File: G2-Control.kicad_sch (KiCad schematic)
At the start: 96 parts, among them J1 Conn_01x06_Pin, J102 Conn_01x06_Pin, J103 Conn_01x06_Pin, J104 Board Interconnect, J2 Q2_link, J3 Conn_01x07_Pin, J4 Conn_01x05_Pin, K1 AZ822-2C-24DSE, K2 AZ822-2C-24DSE, K3 AZ822-2C-24DSE, Q1 TIP122, Q2 IRF840BPF, Q3 2N5061, Q4 2N4403, Q5 BC847, Q6 IRF9530N, U1 LM317L_SOT89, U2 uA748, U3 4N36, U4 78L05, U5 LMC555CMX

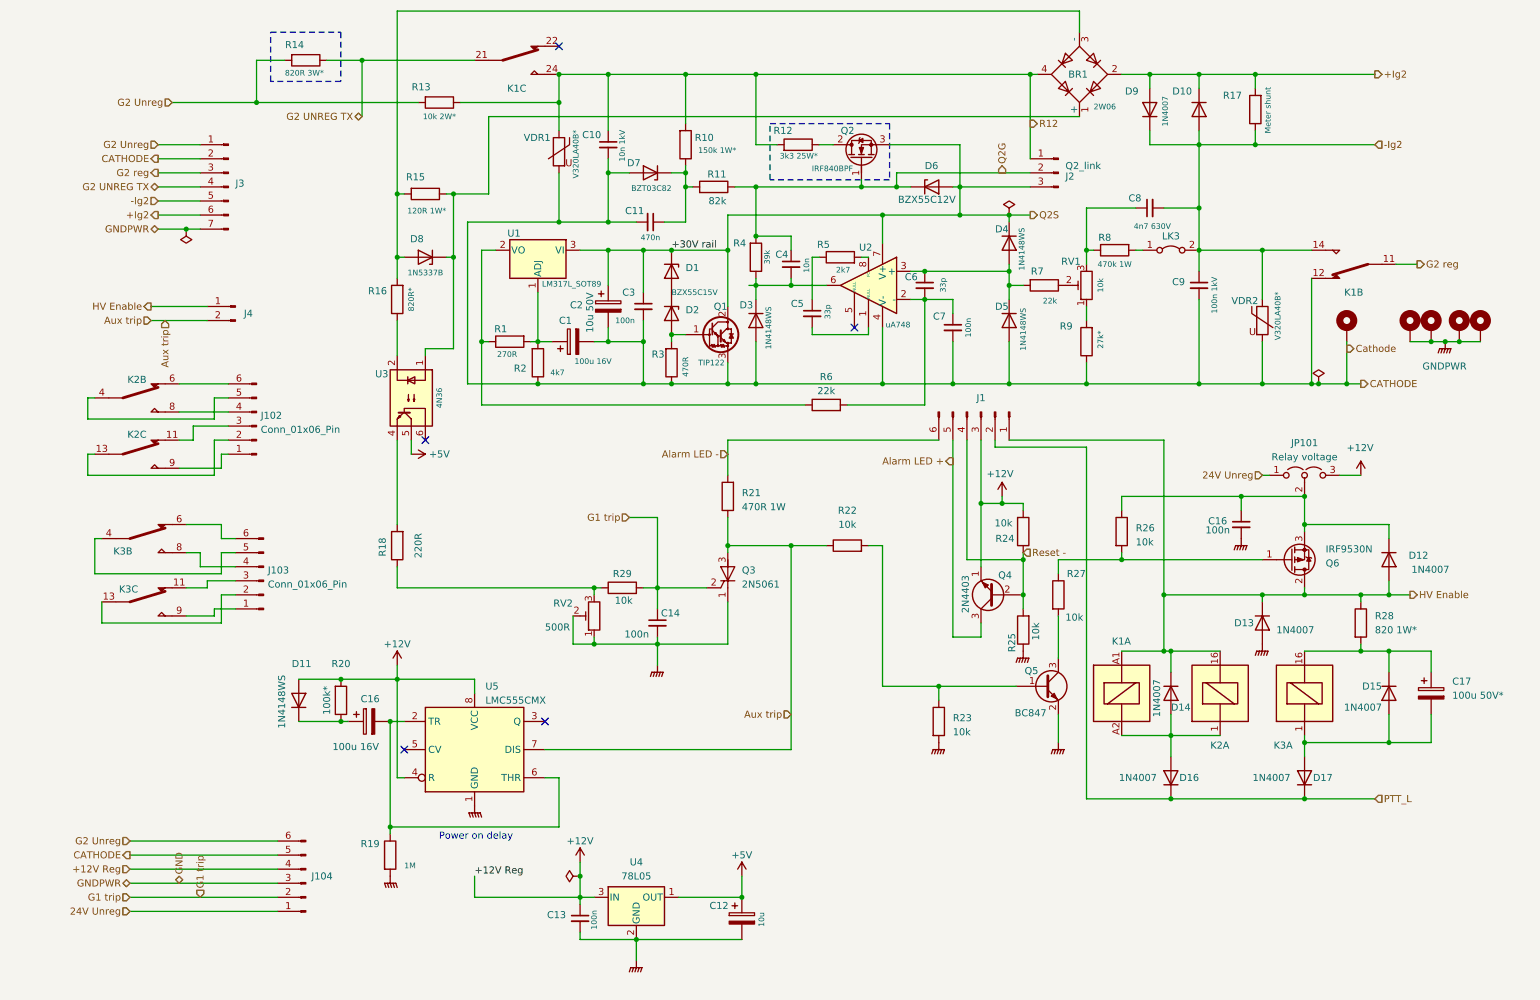
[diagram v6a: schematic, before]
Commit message: Updated format to KiCad 9. Included footprints etc.
Standardized PCB layers, updated property formatting, and adjusted net assignments. Added some DigiKey, Electrokit, and Mouser component part numbers.
Reduced font sizes for better readability and incorporated embedded font settings.
Removed the sequencer from the schematic which wasn't really meant to be there.
Revised and excluded drc and erc warnings and exclusions.
Included footprints into the project library that formerly was defined outside of the project.
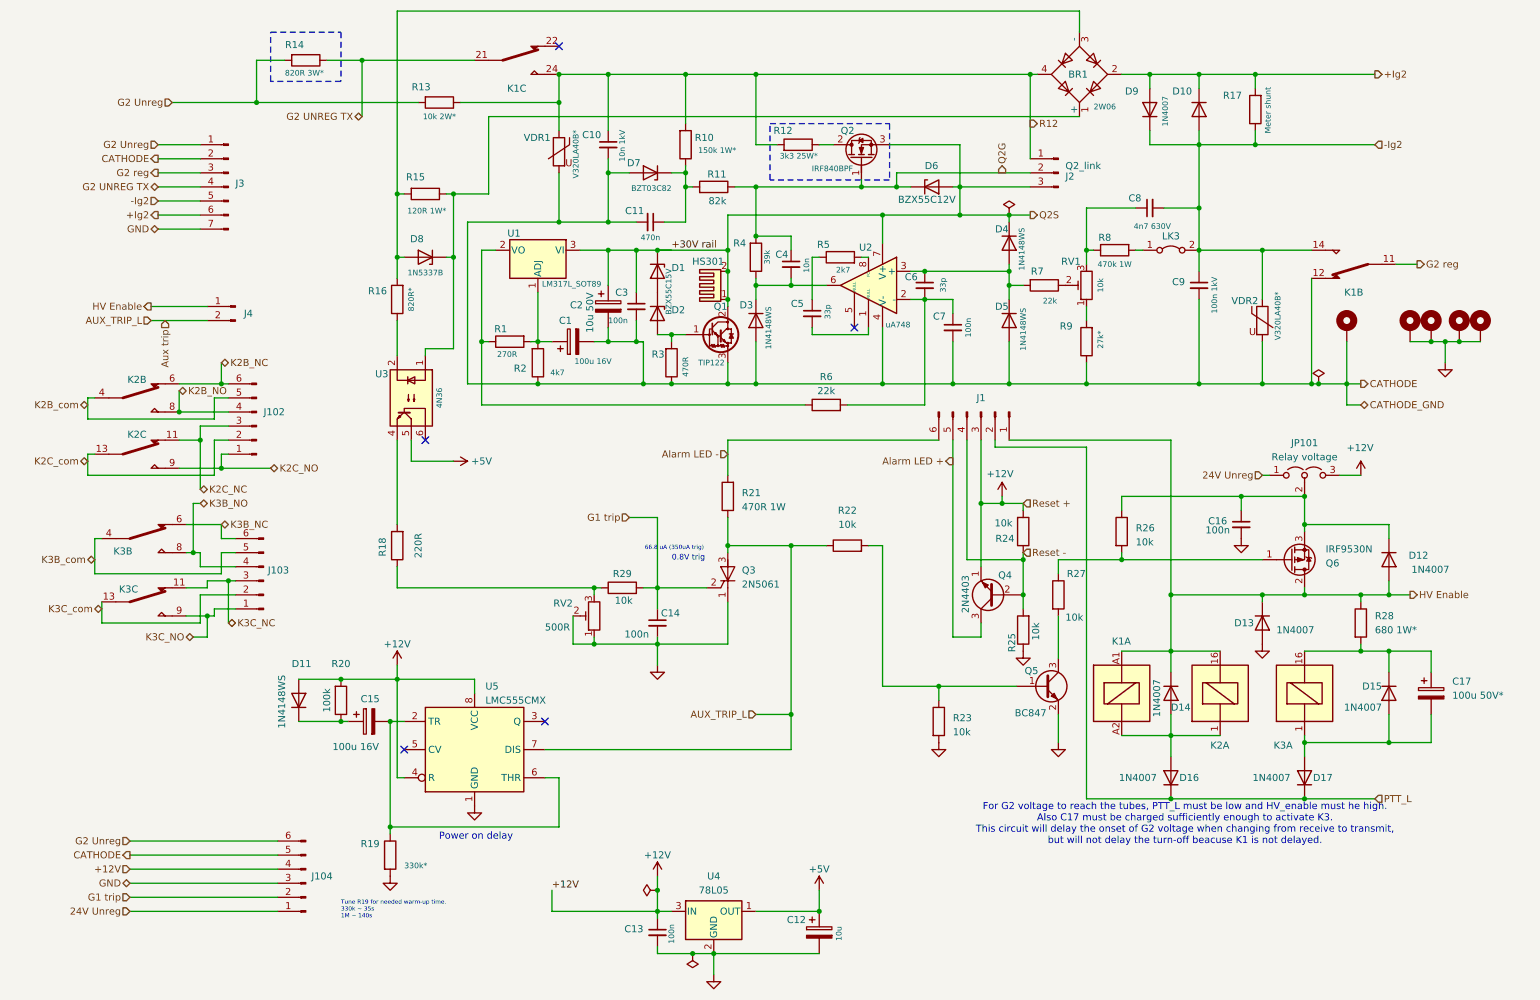
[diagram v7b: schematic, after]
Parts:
- added HS301: Heatsink_Pad_2Pin, Project_library:6025DG_Cooler, symbol Mechanical:Heatsink_Pad_2Pin
- BR1: Electrokit # (none) -> 40310051; Order # 40310051 -> (none); SMD (none) -> 0; Supplier Electrokit -> (none)
- C1: Electrokit # (none) -> 41013566; Order # 41013566 -> (none); SMD (none) -> 1; Supplier Electrokit -> (none)
- C10: Electrokit # (none) -> 41015195; Order # 41015195 -> (none); SMD (none) -> 0; Supplier Electrokit -> (none)
- C11: Electrokit # (none) -> 40502115; Mouser # (none) -> 963-HMK212C7474MGHTE; Order # 40502115 -> (none); SMD (none) -> 1; Supplier Electrokit -> (none)
- C12: Electrokit # (none) -> 40503063; Mouser # (none) -> 187-CL31A106KAHNFNE; Order # 40503063 -> (none); SMD (none) -> 1; Supplier Electrokit -> (none)
- C13, C14, C16, C3, C7: Electrokit # (none) -> 40503054; Mouser # (none) -> 80-C1206C104M5R; Order # 40503054 -> (none); SMD (none) -> 1; Supplier Electrokit -> (none)
- C15: renamed from C16; Electrokit # (none) -> 41013566; Order # 41013566 -> (none); SMD (none) -> 1; Supplier Electrokit -> (none)
- C17: SMD (none) -> 0; Supplier Electrokit* -> (none)
- C2: Electrokit # (none) -> 41015482; Order # 41015482 -> (none); SMD (none) -> 1; Supplier Electrokit -> (none)
- C4: Electrokit # (none) -> 40502095; Order # 40502095 -> (none); SMD (none) -> 1; Supplier Electrokit -> (none)
- C5, C6: Electrokit # (none) -> 40502045; Order # 40502045 -> (none); SMD (none) -> 1; Supplier Electrokit -> (none)
- C8: Electrokit # (none) -> 41016833; Order # 41016833 -> (none); SMD (none) -> 0; Supplier Electrokit -> (none)
- C9: Electrokit # (none) -> 41016939; Order # 41016939 -> (none); SMD (none) -> 0; Supplier Electrokit -> (none)
- D1, D2: Electrokit # (none) -> 40310036; Order # 40310036 -> (none); SMD (none) -> 0; Supplier Electrokit -> (none)
- D10, D12, D13, D14, D15, D16, D17, D9: Electrokit # (none) -> 40310007; Order # 40310007 -> (none); SMD (none) -> 0; Supplier Electrokit -> (none)
- D11, D3, D4, D5: Electrokit # (none) -> 41011670; Order # 41011670 -> (none); SMD (none) -> 1; Supplier Electrokit -> (none)
- D6: Electrokit # (none) -> 40310033; Order # 40310033 -> (none); SMD (none) -> 0; Supplier Electrokit -> (none)
- D7: DigiKey # (none) -> 112-BZT03C82-CT-ND; Order # 112-BZT03C82-CT-ND -> (none); SMD (none) -> 0; Supplier DigiKey -> (none)
- D8: DigiKey # (none) -> 1N5337BGOS-ND; Order # 1N5337BGOS-ND -> (none); SMD (none) -> 0; Supplier DigiKey -> (none)
- H1, H2, H3, H4, H5: Electrokit # (none) -> ----; Order # ---- -> (none); SMD (none) -> 0; Supplier Elecrow -> (none)
- J1, J102, J103: Electrokit # (none) -> 41017488; Order # 41017488 -> (none); SMD (none) -> 0; Supplier Electrokit -> (none)
- J104: value Board Interconnect -> Board Interconnect; Electrokit # (none) -> 41017488; Order # 41017488 -> (none); SMD (none) -> 0; Supplier Electrokit -> (none)
- J2: Electrokit # (none) -> 40210022; Order # 40210022 -> (none); SMD (none) -> 0; Supplier Electrokit -> (none)
- J3: DigiKey # (none) -> 277-1155-ND; Order # 277-1155-ND -> (none); SMD (none) -> 0; Supplier DigiKey -> (none)
- J4: Electrokit # (none) -> 40210021; Order # 40210021 -> (none); SMD (none) -> 0; Supplier Electrokit -> (none)
- JP101: Electrokit # (none) -> 41010445; Order # 41010445 -> (none); SMD (none) -> 0; Supplier Electrokit -> (none)
- K1: value AZ822-2C-24DSE -> Schrack RTE24024; Electrokit # (none) -> 41016807; Mouser # (none) -> 655-RTE24024; Order # 3385-AZ822-2C-24DSE-ND -> (none); SMD (none) -> 0; Supplier DigiKey -> (none)
- K2: DigiKey # (none) -> 3385-AZ822-2C-24DSE-ND; Order # 3385-AZ822-2C-24DSE-ND -> (none); SMD (none) -> 0; Supplier DigiKey -> (none)
- K3: SMD (none) -> 0
- LK3: Electrokit # (none) -> ----; Order # ---- -> (none); SMD (none) -> 0; Supplier Me (wire) -> (none)
- Q1: Electrokit # (none) -> 40320122; Order # 40320122 -> (none); SMD (none) -> 0; Supplier Electrokit -> (none)
- Q2: Electrokit # (none) -> 41011818; Order # 41011818 -> (none); SMD (none) -> 0; Supplier Electrokit -> (none)
- Q3: footprint Package_TO_SOT_THT:TO-92S_Wide -> Project_library:TO-92S_Wide; Electrokit # (none) -> 41017550; Order # 41017550 -> (none); SMD (none) -> 0; Supplier Electrokit -> (none)
- Q4: Electrokit # (none) -> 41011150; Order # 41011150 -> (none); SMD (none) -> 0; Supplier Electrokit -> (none)
- Q5: Electrokit # (none) -> 40320013; Order # 40320013 -> (none); SMD (none) -> 1; Supplier Electrokit -> (none)
- Q6: Electrokit # (none) -> 41015917; Order # 41015917 -> (none); SMD (none) -> 0; Supplier Electrokit -> (none)
- R1: Electrokit # (none) -> 40818227; Order # 40818227 -> (none); SMD (none) -> 1; Supplier Electrokit -> (none)
- R10: DigiKey # (none) -> 150KWCT-ND; Order # 150KWCT-ND -> (none); SMD (none) -> 0; Supplier DigiKey -> (none)
- R11: Electrokit # (none) -> 40818482; Mouser # (none) -> 667-ERJ-P08J823V; Order # 40818482 -> (none); SMD (none) -> 1; Supplier Electrokit -> (none)
- R12: DigiKey # (none) -> A132004-ND; Order # A132004-ND -> (none); SMD (none) -> 0; Supplier DigiKey -> (none)
- R13: DigiKey # (none) -> 10KZCT-ND; Order # 10KZCT-ND -> (none); SMD (none) -> 0; Supplier DigiKey -> (none)
- R14: DigiKey # (none) -> KAL50FB1K00-ND*; Order # KAL50FB1K00-ND* -> (none); SMD (none) -> 0; Supplier DigiKey* -> (none)
- R15: DigiKey # (none) -> PPC82W-1CT-ND* KAL50FB1K00-ND* F3039-ND LMC555CMXCT-ND 296-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; Order # PPC82W-1CT-ND* -> (none); SMD (none) -> 0; Supplier DigiKey* -> (none)
- R16: Electrokit # (none) -> 40818315; Order # 40818315 -> (none); SMD (none) -> 1; Supplier Electrokit -> (none)
- R17: SMD (none) -> 1
- R18: Electrokit # (none) -> 40818222; Order # 40818222 -> (none); SMD (none) -> 1; Supplier Electrokit -> (none)
- R19: value 1M -> 330k*; Electrokit # (none) -> 40818610; Mouser # (none) -> 279-CRGP1206F1M0; Order # 40818610 -> (none); SMD (none) -> 1; Supplier Electrokit -> (none)
- R2: Electrokit # (none) -> 40818347; Mouser # (none) -> 603-RC1206FR-074K7L; Order # 40818347 -> (none); SMD (none) -> 1; Supplier Electrokit -> (none)
- R20: value 100k* -> 100k; Electrokit # (none) -> 40818510; Order # 40818510 -> (none); SMD (none) -> 1; Supplier Electrokit -> (none)
- R21: DigiKey # (none) -> 13-FMP100JT-52-470RCT-ND; Order # 13-FMP100JT-52-470RCT-ND -> (none); SMD (none) -> 0; Supplier DigiKey -> (none)
- R22, R23, R24, R25, R26, R27, R29: Electrokit # (none) -> 40818410; Order # 40818410 -> (none); SMD (none) -> 1; Supplier Electrokit -> (none)
- R28: value 820 1W* -> 680 1W*; SMD (none) -> 0
- R3: Electrokit # (none) -> 40818247; Mouser # (none) -> 603-AF1206JR-07470RL; Order # 40818247 -> (none); SMD (none) -> 1; Supplier Electrokit -> (none)
- R4: Electrokit # (none) -> 40818439; Mouser # (none) -> 603-RC1206JR-0739KL; Order # 40818439 -> (none); SMD (none) -> 1; Supplier Electrokit -> (none)
- R5: Electrokit # (none) -> 40818327; Mouser # (none) -> 652-CR1206FX-2701ELF; Order # 40818327 -> (none); SMD (none) -> 1; Supplier Electrokit -> (none)
- R6, R7: Electrokit # (none) -> 40818422; Mouser # (none) -> 71-CRCW1206-22K-E3; Order # 40818422 -> (none); SMD (none) -> 1; Supplier Electrokit -> (none)
- R8: DigiKey # (none) -> 470KWCT-ND; Order # 470KWCT-ND -> (none); SMD (none) -> 0; Supplier DigiKey -> (none)
- R9: Electrokit # (none) -> 40818427; Mouser # (none) -> 708-RMCF1206FT27K0; Order # 40818427 -> (none); SMD (none) -> 1; Supplier Electrokit -> (none)
- RV1: Electrokit # (none) -> 40900227; Order # 40900227 -> (none); SMD (none) -> 0; Supplier Electrokit -> (none)
- RV2: Electrokit # (none) -> 40900223; Order # 40900223 -> (none); SMD (none) -> 0; Supplier Electrokit -> (none)
- U1: DigiKey # (none) -> 296-26093-1-ND; Order # 296-26093-1-ND -> (none); SMD (none) -> 1; Supplier DigiKey -> (none)
- U2: SMD (none) -> 0; Supplier Me or eBay -> (none)
- U3: footprint Package_SO:SOP-6_6.62x6.62mm_P2.54mm -> Project_library:SOP-6_6.62x6.62mm_P2.54mm; Electrokit # (none) -> 41011130; Order # 41011130 -> (none); SMD (none) -> 0; Supplier Electrokit -> (none)
- U4: Electrokit # (none) -> 41016543; Order # 41016543 -> (none); SMD (none) -> 1; Supplier Electrokit -> (none)
- U5: DigiKey # (none) -> LMC555CMXCT-ND; Order # LMC555CMXCT-ND -> (none); SMD (none) -> 1; Supplier DigiKey -> (none)
- VDR1, VDR2: DigiKey # (none) -> F3039-ND; Order # F3039-ND -> (none); SMD (none) -> 0; Supplier DigiKey -> (none)
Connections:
- net Q2S: now also HS301.1, HS301.2
- net K3B_com: now reaches J103.5 (Pin_5), K3.4
- net K3B_NC: now reaches J103.6 (Pin_6), K3.6
- net K3B_NO: now reaches J103.4 (Pin_4), K3.8
- net K2B_com: now reaches J102.5 (Pin_5), K2.4
- net K2B_NC: now reaches J102.6 (Pin_6), K2.6
- net K2B_NO: now reaches J102.4 (Pin_4), K2.8
- net K2C_NC: now reaches J102.3 (Pin_3), K2.11
- net K2C_com: now reaches J102.2 (Pin_2), K2.13
- net K2C_NO: now reaches J102.1 (Pin_1), K2.9
- net K3C_NC: now reaches J103.3 (Pin_3), K3.11
- net K3C_com: now reaches J103.2 (Pin_2), K3.13
- net K3C_NO: now reaches J103.1 (Pin_1), K3.9
- net Aux trip renamed AUX_TRIP_L
- net GNDPWR renamed GND
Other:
- note added: "0.8V trig"
- note added: "66.8 uA (350uA trig)"
- note added: "For G2 voltage to reach the tubes, PTT_L must be low and HV_enable must he high. Also C17 must be charged sufficiently enough to activate K3. This circuit will delay the onset of G2 voltage when changing from receive to transmit, but will not delay the turn-off beacuse K1 is not delayed."
- note added: "Tune R19 for needed warm-up time. 330k ~ 35s 1M ~ 140s"
- moved on the sheet: C12, C13, C3, D1, D2, U4
